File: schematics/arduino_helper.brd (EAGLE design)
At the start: 54 x 18 mm, 8 parts, among them Q1 L78M05CDT

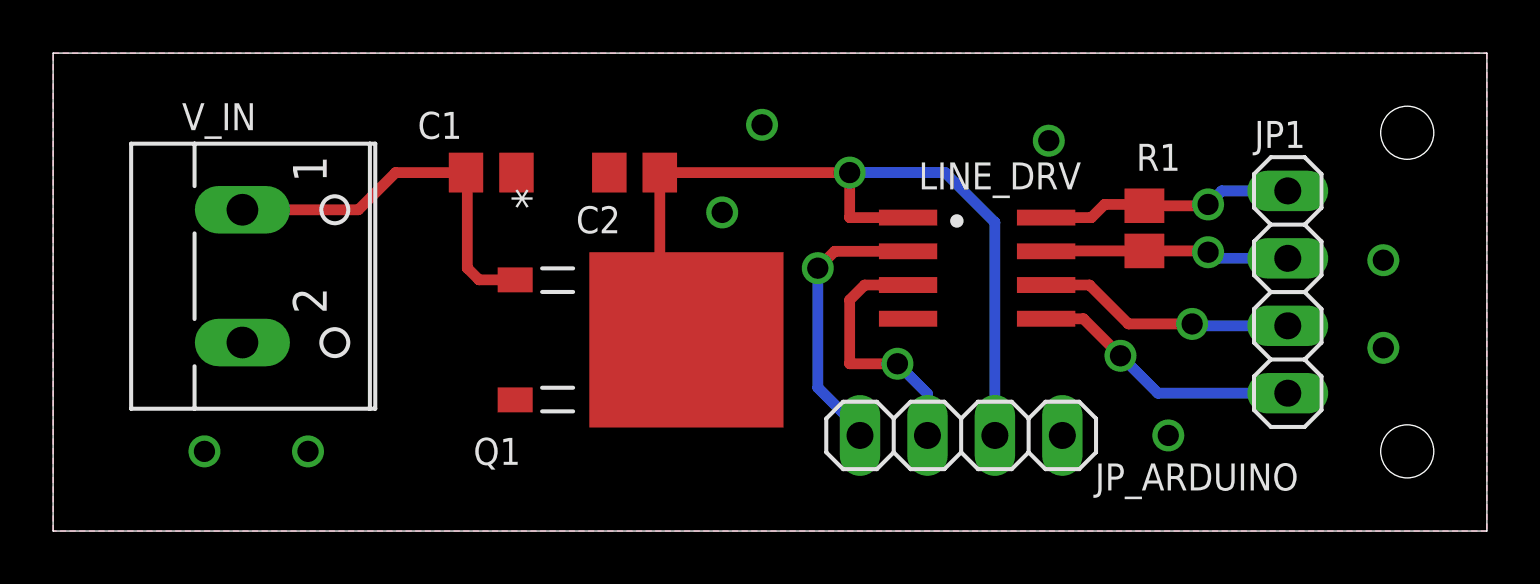
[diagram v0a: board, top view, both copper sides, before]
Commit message: Extra caps, wider supply traces for the Arduino helper PCB.
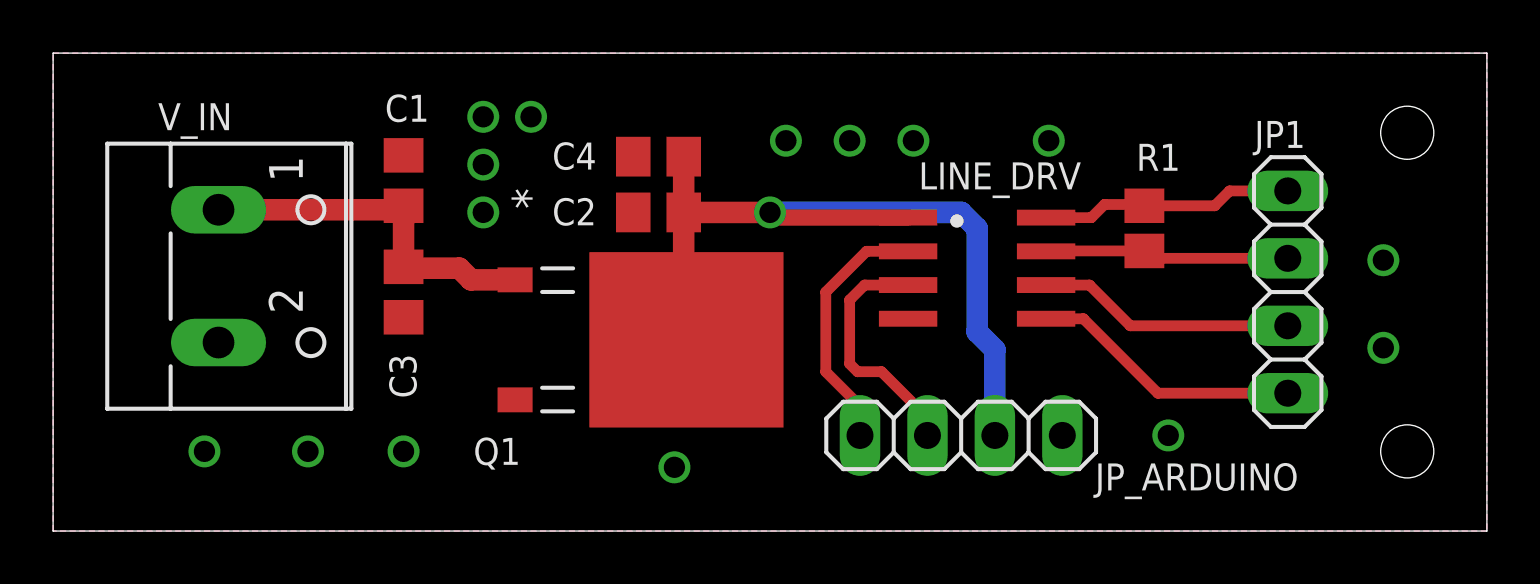
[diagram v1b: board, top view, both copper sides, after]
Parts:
- added C3, C4: 1uF, rcl:C0805
- moved C1 3.31 mm to (13.2, 13.2), turned to 90 degrees
- moved C2 1.75 mm to (22.8, 12.0)
- moved V_IN 0.90 mm to (7.50, 9.60)
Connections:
- net +12V: now also C3.1
- net GND: now also C3.2, C4.2
- net VCC: now also C4.1
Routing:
- net VCC: track 32.0 -> 33.0 mm
- net RXD: track 10.6 -> 9.67 mm, vias 1 -> 0
- net +12V: track 14.6 -> 13.7 mm
- net TXD: track 9.80 -> 9.27 mm, vias 1 -> 0
- net N$2: vias 1 -> 0
- net N$1: vias 1 -> 0
- net N$4: vias 1 -> 0
- net N$3: vias 1 -> 0

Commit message: Added names to unnamed signals.
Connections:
- net N$1 renamed RI-
- net N$2 renamed RI+
- net N$3 renamed DO-
- net N$4 renamed DO+
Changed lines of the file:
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@@
 </elements>
 <signals>
-<signal name="N$1">
+<signal name="RI-">
 <contactref element="LINE_DRV" pad="7"/>
 <contactref element="R1" pad="1"/>
@@
 <wire x1="41.38" y1="10.27" x2="41.1" y2="10.55" width="0.4064" layer="1"/>
 </signal>
-<signal name="N$2">
+<signal name="RI+">
 <contactref element="LINE_DRV" pad="8"/>
 <contactref element="R1" pad="2"/>
@@
 <wire x1="46.5" y1="12.81" x2="44.31" y2="12.81" width="0.4064" layer="1"/>
 </signal>
-<signal name="N$3">
+<signal name="DO-">
 <contactref element="LINE_DRV" pad="5"/>
 <contactref element="JP1" pad="4"/>
@@
 <wire x1="41.61" y1="5.19" x2="38.805" y2="7.995" width="0.4064" layer="1"/>
 </signal>
-<signal name="N$4">
+<signal name="DO+">
 <contactref element="LINE_DRV" pad="6"/>
 <contactref element="JP1" pad="3"/>
